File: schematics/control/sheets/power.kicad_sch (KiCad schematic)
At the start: 12 parts, among them U16 L7905, U6 L7805

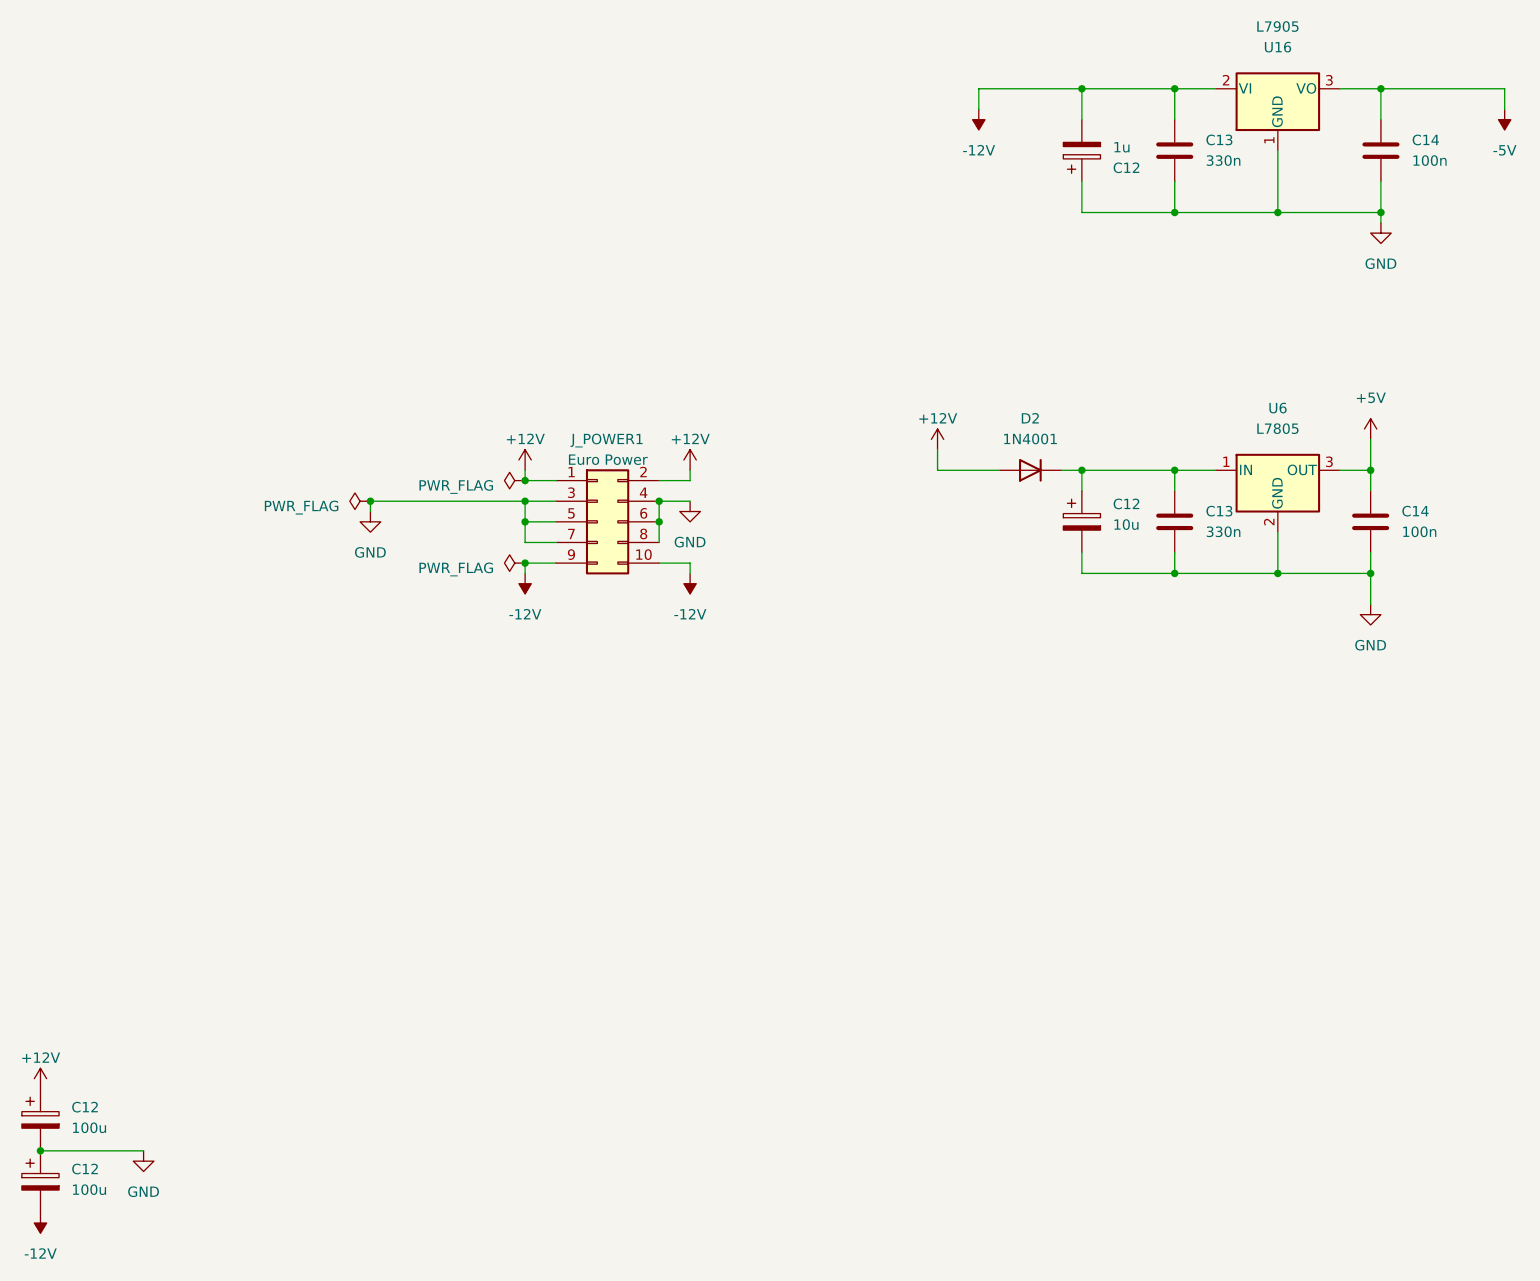
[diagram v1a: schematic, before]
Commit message: Added pulse width mod schematics
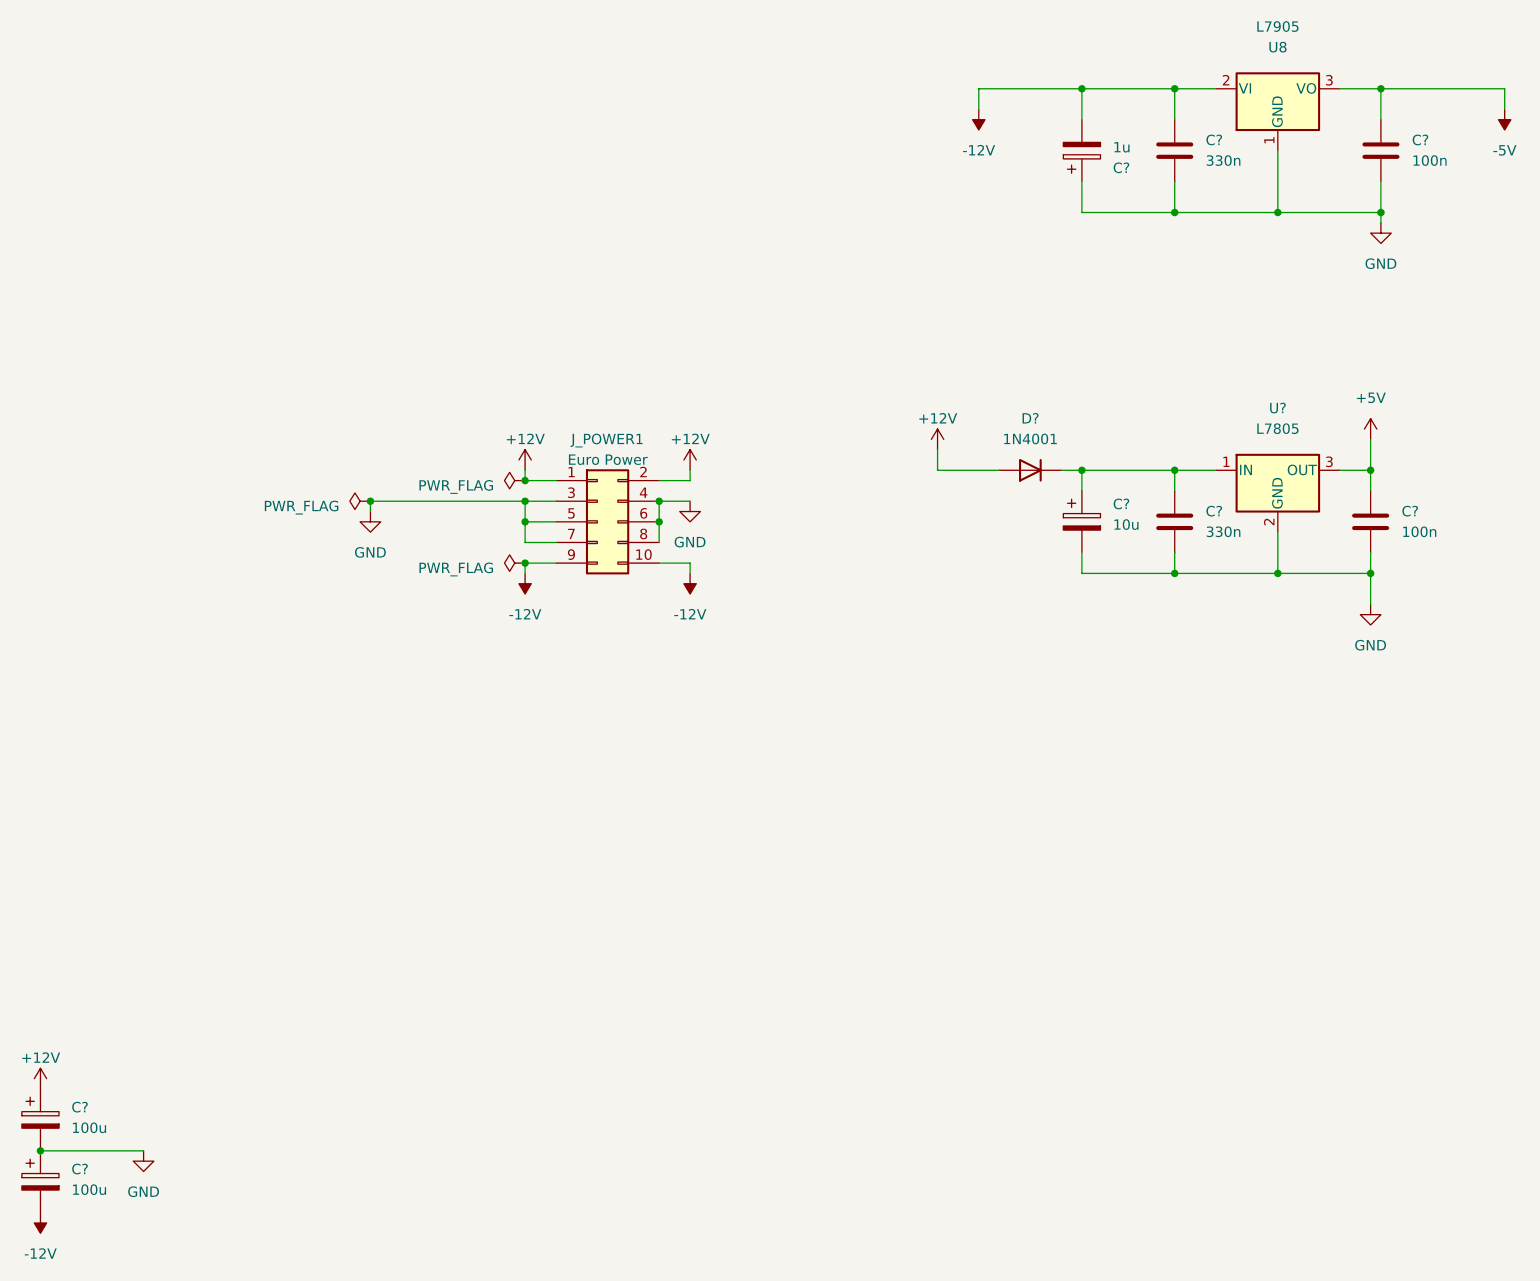
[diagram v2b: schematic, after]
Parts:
- renumbered C14 to C?, C12 to C?, C13 to C?, D2 to D?, U16 to U8, U6 to U?

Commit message: Updated VCA
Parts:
- added J_PANEL_GND: Conn_01x03_Pin, symbol Connector:Conn_01x03_Pin
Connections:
- net GND: now also J_PANEL_GND.1 (Pin_1), J_PANEL_GND.2 (Pin_2), J_PANEL_GND.3 (Pin_3)
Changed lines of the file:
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@@
   (junction (at 166.37 63.5) (diameter 0) (color 0 0 0 0)
   )
+  (junction (at 129.54 129.54) (diameter 0) (color 0 0 0 0)
+  )
   (junction (at 190.5 95.25) (diameter 0) (color 0 0 0 0)
   )
+  (junction (at 129.54 132.08) (diameter 0) (color 0 0 0 0)
+  )
   (junction (at 102.87 101.6) (diameter 0) (color 0 0 0 0)
   )
@@
     (stroke (width 0) (type default))
   )
+  (wire (pts (xy 129.54 132.08) (xy 129.54 129.54))
+    (stroke (width 0) (type default))
+  )
   (wire (pts (xy 137.16 92.71) (xy 137.16 95.25))
     (stroke (width 0) (type default))
@@
     (stroke (width 0) (type default))
   )
+  (wire (pts (xy 129.54 134.62) (xy 129.54 132.08))
+    (stroke (width 0) (type default))
+  )
   (wire (pts (xy 166.37 48.26) (xy 154.94 48.26))
     (stroke (width 0) (type default))
@@
     (stroke (width 0) (type default))
   )
+  (wire (pts (xy 123.19 132.08) (xy 129.54 132.08))
+    (stroke (width 0) (type default))
+  )
   (wire (pts (xy 186.69 95.25) (xy 190.5 95.25))
     (stroke (width 0) (type default))
@@
     (stroke (width 0) (type default))
   )
+  (wire (pts (xy 129.54 129.54) (xy 129.54 127))
+    (stroke (width 0) (type default))
+  )
   (wire (pts (xy 191.77 64.77) (xy 191.77 63.5))
     (stroke (width 0) (type default))
   )
+  (wire (pts (xy 129.54 127) (xy 123.19 127))
+    (stroke (width 0) (type default))
+  )
   (wire (pts (xy 67.31 99.06) (xy 86.36 99.06))
     (stroke (width 0) (type default))
@@
   )
   (wire (pts (xy 179.07 63.5) (xy 166.37 63.5))
+    (stroke (width 0) (type default))
+  )
+  (wire (pts (xy 123.19 129.54) (xy 129.54 129.54))
     (stroke (width 0) (type default))
   )
@@
     )
   )
+  (symbol (lib_id "Connector:Conn_01x03_Pin") (at 118.11 129.54 0) (unit 1)
+    (in_bom yes) (on_board yes) (dnp no) (fields_autoplaced)
+    (property "Reference" "J_PANEL_GND" (at 118.745 123.19 0)
+      (effects (font (size 1.27 1.27)))
+    )
+    (property "Value" "Conn_01x03_Pin" (at 118.745 125.73 0)
+      (effects (font (size 1.27 1.27)))
+    )
+    (property "Footprint" "" (at 118.11 129.54 0)
+      (effects (font (size 1.27 1.27)) hide)
+    )
+    (property "Datasheet" "~" (at 118.11 129.54 0)
+      (effects (font (size 1.27 1.27)) hide)
+    )
+    (pin "1")
+    (pin "2")
+    (pin "3")
+    (instances
+      (project "shmoergh-funk-live-control"
+        (path "/6d7b782d-8b2e-4b40-a99f-4bf41187d978/42407d8b-94dc-4f64-92f9-b98d15e7f7d8"
+          (reference "J_PANEL_GND") (unit 1)
+        )
+      )
+    )
+  )
   (symbol (lib_id "power:GND") (at 191.77 64.77 0) (unit 1)
     (in_bom yes) (on_board yes) (dnp no) (fields_autoplaced)
@@
         )
       )
+    )
+  )
+  (symbol (lib_id "power:GND") (at 129.54 134.62 0) (unit 1)
+    (in_bom yes) (on_board yes) (dnp no) (fields_autoplaced)
+    (property "Reference" "#PWR0101" (at 129.54 140.97 0)
+      (effects (font (size 1.27 1.27)) hide)
+    )
+    (property "Value" "GND" (at 129.54 139.7 0)
+      (effects (font (size 1.27 1.27)))
+    )
+    (property "Footprint" "" (at 129.54 134.62 0)
+      (effects (font (size 1.27 1.27)) hide)
+    )
+    (property "Datasheet" "" (at 129.54 134.62 0)
+      (effects (font (size 1.27 1.27)) hide)
+    )
+    (pin "1")
+    (instances
+      (project "shmoergh-funk-live-control"
+        (path "/6d7b782d-8b2e-4b40-a99f-4bf41187d978/42407d8b-94dc-4f64-92f9-b98d15e7f7d8"
+          (reference "#PWR0101") (unit 1)
+        )
+      )

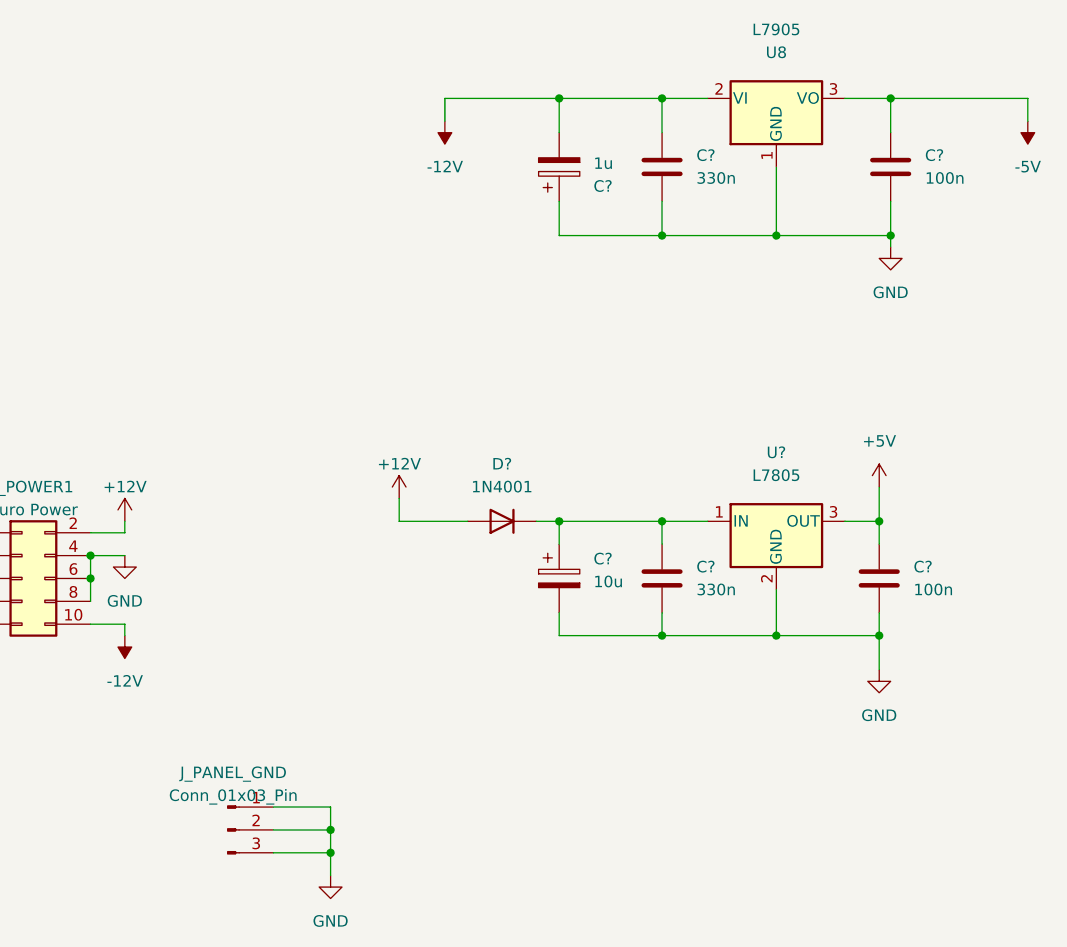
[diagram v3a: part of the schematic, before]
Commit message: Added all UI components to schematics
- digital UI
- filter UI
- updated voice interface connection
- simplified schematics a lot
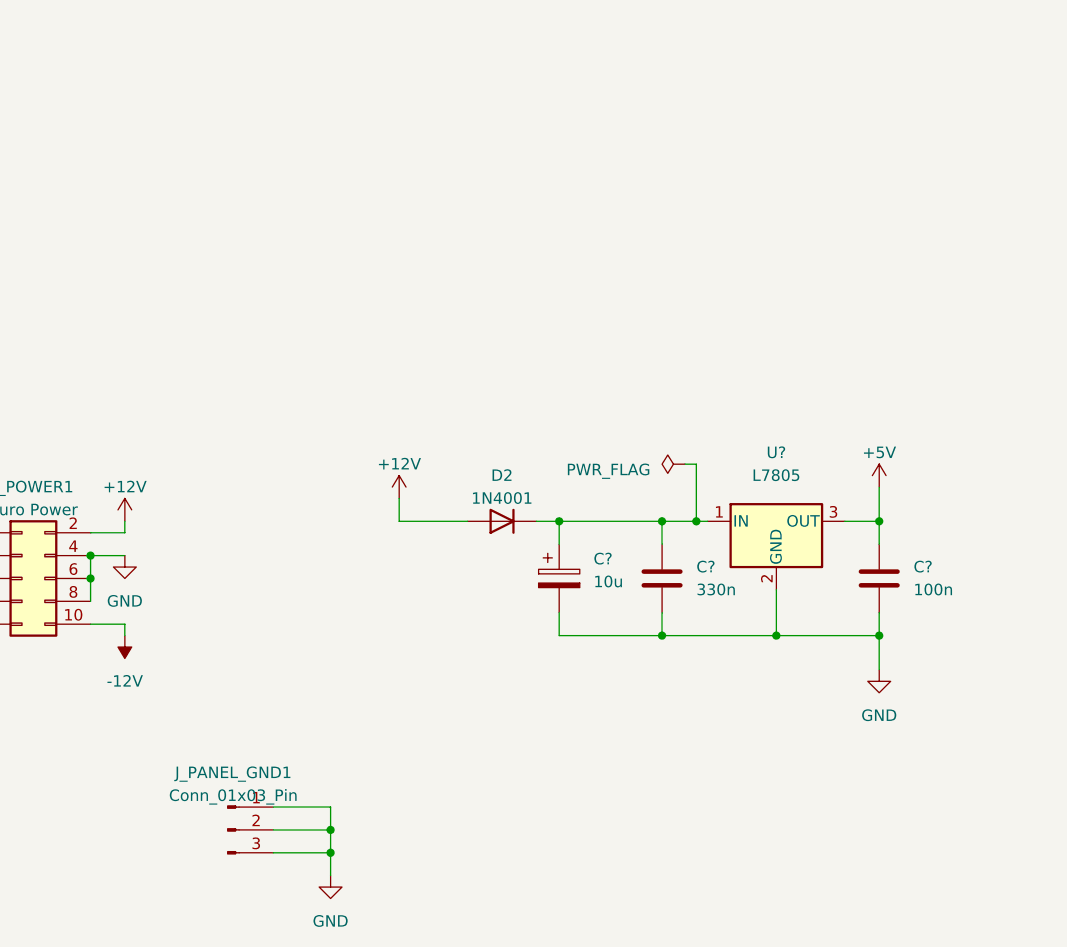
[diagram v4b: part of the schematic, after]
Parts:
- removed C?: 100n, Capacitor_THT:C_Disc_D3.0mm_W2.0mm_P2.50mm, symbol Device:C
- removed C?: 1u, Capacitor_THT:CP_Radial_D6.3mm_P2.50mm, symbol Device:C_Polarized
- removed C?: 330n, Capacitor_THT:C_Disc_D3.0mm_W2.0mm_P2.50mm, symbol Device:C
- removed D?: 1N4001, Diode_THT:D_DO-41_SOD81_P10.16mm_Horizontal, symbol Diode:1N4001
- removed U8: L7905, Package_TO_SOT_THT:TO-220-3_Vertical, symbol Regulator_Linear:L7905
- added D2: 1N4001, symbol Device:D
- C? (x2): footprint Capacitor_THT:C_Disc_D3.0mm_W2.0mm_P2.50mm -> (none)
- C? (x3): footprint Capacitor_THT:CP_Radial_D6.3mm_P2.50mm -> (none)
- J_POWER1: footprint Connector_IDC:IDC-Header_2x05_P2.54mm_Vertical -> (none)
- U?: footprint Package_TO_SOT_THT:TO-220-3_Vertical -> (none)
- renumbered J_PANEL_GND to J_PANEL_GND1
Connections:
- net +12V: now also D2.2 (A)
- net at C?.1, C?.1, U?.1 (IN): now also D2.1 (K)

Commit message: Schemo work
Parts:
- added JP_INTERNAL_VCA_GATE1: jmpr, PCM_Jumper_AKL_Double:Jumper_P2.54mm_D0.7mm, symbol Jumper:Jumper_2_Open
- C? (x2): footprint (none) -> Capacitor_THT:C_Disc_D3.0mm_W2.0mm_P2.50mm
- C? (x3): footprint (none) -> Capacitor_THT:CP_Radial_D6.3mm_P2.50mm
- D2: footprint (none) -> Diode_THT:D_DO-41_SOD81_P7.62mm_Horizontal
- J_PANEL_GND1: footprint (none) -> Shmoergh_Custom_Footprints:NSL25_01x03_Vertical
- J_POWER1: footprint (none) -> Connector_IDC:IDC-Header_2x05_P2.54mm_Vertical
- U?: footprint (none) -> PCM_Package_TO_SOT_THT_AKL:TO-220-3_Vertical
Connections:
- net +12V: now also J_POWER1.10 (Pin_10), J_POWER1.9 (Pin_9), JP_INTERNAL_VCA_GATE1.1 (A); no longer D2.2 (A), J_POWER1.1 (Pin_1), J_POWER1.2 (Pin_2)
- net -12V: now also J_POWER1.1 (Pin_1), J_POWER1.2 (Pin_2); no longer J_POWER1.10 (Pin_10), J_POWER1.9 (Pin_9)
- new net: D2.2 (A), JP_INTERNAL_VCA_GATE1.2 (B)
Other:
- note added: "This jumper MUST be removed before flashing!"
